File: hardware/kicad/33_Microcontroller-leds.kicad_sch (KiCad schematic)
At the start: 11 parts, among them U69 74AHCT1G125GW,125-JSM, U70 WS2815F, U71 VH3_96-4P_ZZ

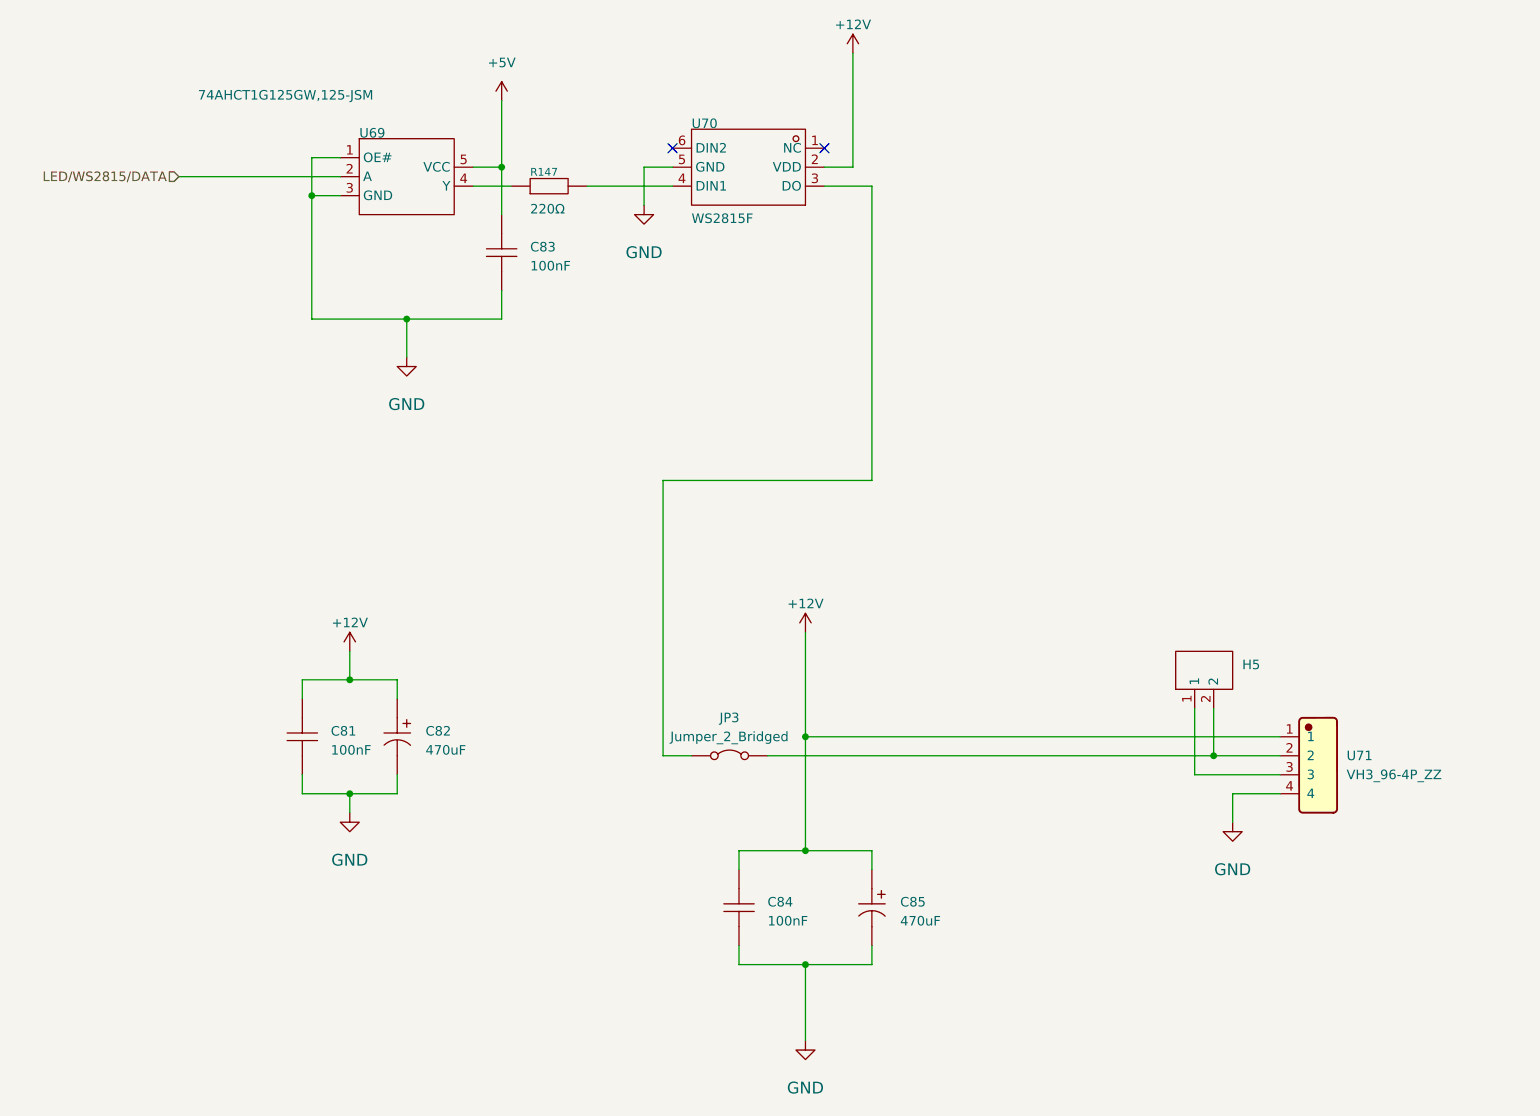
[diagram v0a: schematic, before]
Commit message: new led connector
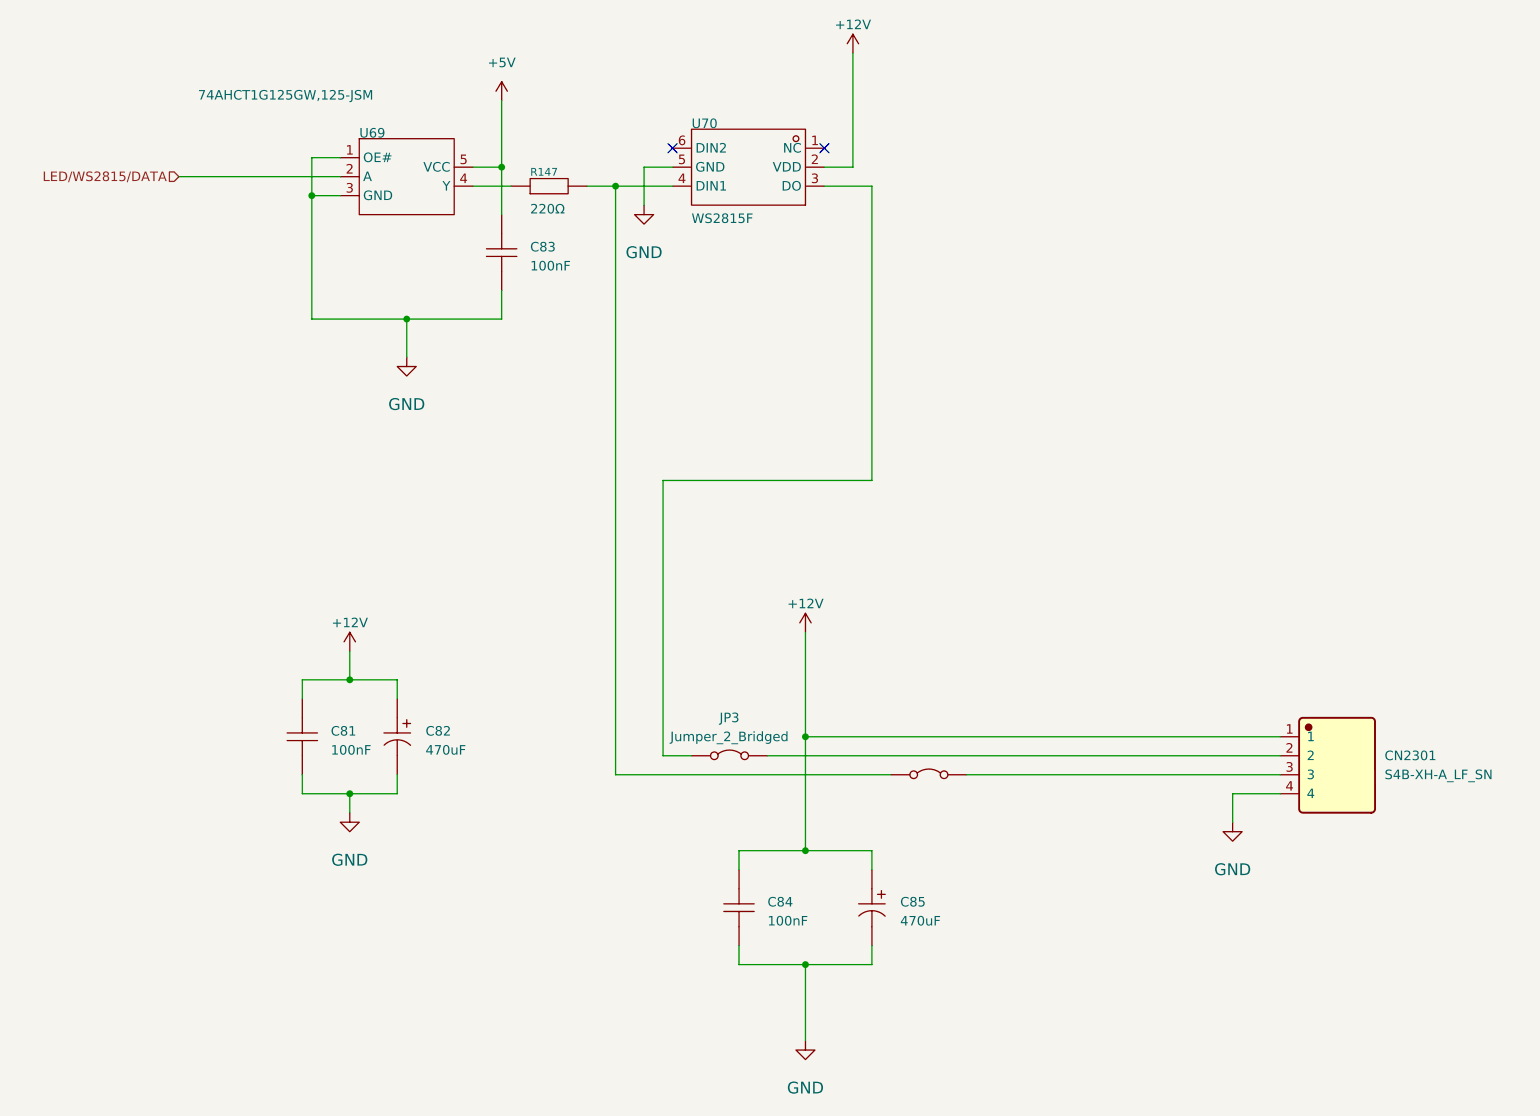
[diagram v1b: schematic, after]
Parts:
- removed H5: PZ254V-11-02P, Connector_PinHeader_2.54mm:PinHeader_1x02_P2.54mm_Vertical, symbol 5v rail sm-easyedapro:PZ254V-11-02P
- removed U71: VH3_96-4P_ZZ, JLCImport:VH3_96-4P_ZZ, symbol JLCImport:VH3_96-4P_ZZ
- added CN2301: S4B-XH-A_LF_SN, JLCImport:S4B-XH-A_LF_SN, symbol JLCImport:S4B-XH-A_LF_SN
- added JP2301: Jumper_2_Bridged, Jumper:SolderJumper-2_P1.3mm_Bridged_RoundedPad1.0x1.5mm, symbol Jumper:Jumper_2_Bridged
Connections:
- net +12V: now also CN2301.1
- net GND: now also CN2301.4
- net at JP3.2 (B): now also CN2301.2
- net at R147.2, U70.4 (DIN1): now also JP2301.1 (A)
- new net: CN2301.3, JP2301.2 (B)

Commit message: starting erc check
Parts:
- C81, C83, C84: footprint Capacitor_SMD:C_0603_1608Metric -> 5v rail sm-easyedapro:C0603
- R147: footprint Resistor_SMD:R_0603_1608Metric -> 5v rail sm-easyedapro:R0603
- U69: footprint Package_TO_SOT_SMD:SOT-353_SC-70-5 -> 5v rail sm-easyedapro:SOT-353_L2.1-W1.3-P0.65-LS2.3-BL
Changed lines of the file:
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@@
 			)
 		)
-		(property "Description" ""
+		(property "Description" "Power symbol creates a global label with name \"GND\" , ground"
 			(at 74.93 78.74 0)
 			(effects
@@
 			)
 		)
-		(property "Description" ""
+		(property "Description" "Power symbol creates a global label with name \"GND\" , ground"
 			(at 67.31 139.7 0)
 			(effects
@@
 			)
 		)
-		(property "Footprint" "Capacitor_SMD:C_0603_1608Metric"
+		(property "Footprint" "5v rail sm-easyedapro:C0603"
 			(at 60.96 129.54 0)
 			(effects
@@
 			)
 		)
-		(property "Footprint" "Package_TO_SOT_SMD:SOT-353_SC-70-5"
+		(property "Footprint" "5v rail sm-easyedapro:SOT-353_L2.1-W1.3-P0.65-LS2.3-BL"
 			(at 74.93 54.61 0)
 			(effects
@@
 			)
 		)
-		(property "Footprint" "Capacitor_SMD:C_0603_1608Metric"
+		(property "Footprint" "5v rail sm-easyedapro:C0603"
 			(at 87.63 64.77 0)
 			(effects
@@
 			)
 		)
-		(property "Footprint" "Resistor_SMD:R_0603_1608Metric"
+		(property "Footprint" "5v rail sm-easyedapro:R0603"
 			(at 93.98 55.88 0)
 			(effects
@@
 			)
 		)
-		(property "Description" ""
+		(property "Description" "Power symbol creates a global label with name \"GND\" , ground"
 			(at 185.42 140.97 0)
 			(effects
@@
 			)
 		)
-		(property "Description" ""
+		(property "Description" "Power symbol creates a global label with name \"GND\" , ground"
 			(at 128.27 170.18 0)
 			(effects
@@
 			)
 		)
-		(property "Footprint" "Capacitor_SMD:C_0603_1608Metric"
+		(property "Footprint" "5v rail sm-easyedapro:C0603"
 			(at 119.38 152.4 0)
 			(effects
@@
 			)
 		)
-		(property "Description" ""
+		(property "Description" "Power symbol creates a global label with name \"GND\" , ground"
 			(at 106.68 58.42 0)
 			(effects

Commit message: leds mostly done
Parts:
- removed C81: 100nF, 5v rail sm-easyedapro:C0603, symbol 5v rail sm-easyedapro:CC0603KRX7R9BB104
- removed C82: 470uF, 5v rail sm-easyedapro:CAP-SMD_BD6.3-L6.6-W6.6-LS7.6-RD, symbol 5v rail sm-easyedapro:RVT1C471M0607
- removed JP2301, JP3: Jumper_2_Bridged, Jumper:SolderJumper-2_P1.3mm_Bridged_RoundedPad1.0x1.5mm, symbol Jumper:Jumper_2_Bridged
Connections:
- net GND: now also C85.2
- net at U70.3 (DO): now also CN2301.3
- no-connect marks 2 -> 3

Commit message: updating symbols to use kicad footprints where possible
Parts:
- C83, C84: footprint 5v rail sm-easyedapro:C0603 -> Capacitor_SMD:C_0603_1608Metric
- R147: footprint 5v rail sm-easyedapro:R0603 -> Resistor_SMD:R_0603_1608Metric
- U69: footprint 5v rail sm-easyedapro:SOT-353_L2.1-W1.3-P0.65-LS2.3-BL -> Package_TO_SOT_SMD:SOT-353_SC-70-5
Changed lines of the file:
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@@
 			)
 		)
-		(property "Footprint" "5v rail sm-easyedapro:SOT-353_L2.1-W1.3-P0.65-LS2.3-BL"
+		(property "Footprint" "Package_TO_SOT_SMD:SOT-353_SC-70-5"
 			(at 74.93 54.61 0)
 			(effects
@@
 			)
 		)
-		(property "Footprint" "5v rail sm-easyedapro:C0603"
+		(property "Footprint" "Capacitor_SMD:C_0603_1608Metric"
 			(at 87.63 64.77 0)
 			(effects
@@
 			)
 		)
-		(property "Footprint" "5v rail sm-easyedapro:R0603"
+		(property "Footprint" "Resistor_SMD:R_0603_1608Metric"
 			(at 93.98 55.88 0)
 			(effects
@@
 			)
 		)
-		(property "Footprint" "5v rail sm-easyedapro:C0603"
+		(property "Footprint" "Capacitor_SMD:C_0603_1608Metric"
 			(at 119.38 152.4 0)
 			(effects

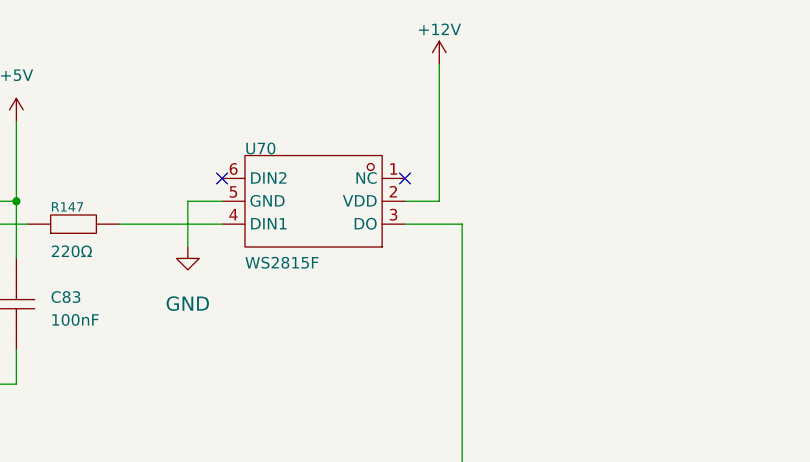
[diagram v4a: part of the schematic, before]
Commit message: starting erc check
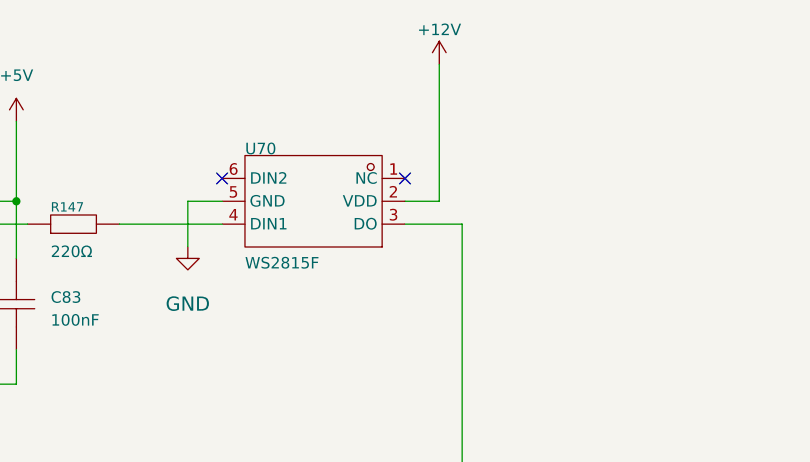
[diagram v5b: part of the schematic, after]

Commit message: more fixes
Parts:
- U70: footprint 5v rail sm-easyedapro:LED-SMD_6P-L5.0-W5.0-TL -> LED_SMD:LED_WS2812_PLCC6_5.0x5.0mm_P1.6mm
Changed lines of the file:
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@@
 			)
 		)
-		(property "Footprint" "5v rail sm-easyedapro:LED-SMD_6P-L5.0-W5.0-TL"
+		(property "Footprint" "LED_SMD:LED_WS2812_PLCC6_5.0x5.0mm_P1.6mm"
 			(at 120.65 53.34 0)
 			(effects

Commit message: update
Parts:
- removed C85: 470uF, 5v rail sm-easyedapro:CAP-SMD_BD6.3-L6.6-W6.6-LS7.6-RD, symbol 5v rail sm-easyedapro:RVT1C471M0607
- added C2301: 189RV0019, JLCImport:189RV0019, symbol JLCImport:189RV0019
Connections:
- net +12V: now also C2301.1
- net GND: now also C2301.2
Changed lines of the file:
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@@
-	)
-	(symbol
-		(lib_id "5v rail sm-easyedapro:RVT1C471M0607")
-		(at 137.16 152.4 270)
-		(unit 1)
-		(exclude_from_sim no)
-		(in_bom yes)
-		(on_board yes)
-		(dnp no)
-		(property "Reference" "C85"
-			(at 140.9446 152.4 90)
-			(effects
-				(font
-					(size 1.27 1.27)
-				)
-				(justify left bottom)
-			)
-		)
-		(property "Value" "470uF"
-			(at 140.9446 154.94 90)
-			(effects
-				(font
-					(size 1.27 1.27)
-				)
-				(justify left bottom)
-			)
-		)
-		(property "Footprint" "5v rail sm-easyedapro:CAP-SMD_BD6.3-L6.6-W6.6-LS7.6-RD"
-			(at 137.16 152.4 0)
-			(effects
-				(font
-					(size 1.27 1.27)
-				)
-				(hide yes)
-			)
-		)
-		(property "Datasheet" ""
-			(at 137.16 152.4 0)
-			(effects
-				(font
-					(size 1.27 1.27)
-				)
-				(hide yes)
-			)
-		)
-		(property "Description" "Capacitance:470uF Tolerance:±20% Tolerance:±20% Voltage Rating:16V Ripple Current:185mA@120Hz Diameter:6.3mm Height - Seated (Max):7.7mm Lifetime:2000hrs@105°C Operating Temperature:-40°C~+105°C Operating Temperature:-40°C~+105°C"
-			(at 137.16 152.4 0)
-			(effects
-				(font
-					(size 1.27 1.27)
-				)
-				(hide yes)
-			)
-		)
-		(property "Manufacturer Part" "RVT1C471M0607"
-			(at 137.16 152.4 0)
-			(effects
-				(font
-					(size 1.27 1.27)
-				)
-				(hide yes)
-			)
-		)
-		(property "Manufacturer" "ROQANG(容强)"
-			(at 137.16 152.4 0)
-			(effects
-				(font
-					(size 1.27 1.27)
-				)
-				(hide yes)
-			)
-		)
-		(property "Supplier Part" "C2977552"
-			(at 137.16 152.4 0)
-			(effects
-				(font
-					(size 1.27 1.27)
-				)
-				(hide yes)
-			)
-		)
-		(property "Supplier" "LCSC"
-			(at 137.16 152.4 0)
-			(effects
-				(font
-					(size 1.27 1.27)
-				)
-				(hide yes)
-			)
-		)
-		(property "LCSC Part Name" "470uF ±20% 16V"
-			(at 137.16 152.4 0)
-			(effects
-				(font
-					(size 1.27 1.27)
-				)
-				(hide yes)
-			)
-		)
-		(pin "1"
-		)
-		(pin "2"
-		)
-		(instances
-			(project "svea_powerboard_rev3"
-				(path "/3f85abf4-0b95-4c4a-b7e9-06f59ca1ea3d/5c2e021f-c2d4-49e2-8c36-9a64f1f12001/c2eb7228-bcb6-49cd-ba01-e5b0712a5c09"
-					(reference "C85")
-					(unit 1)
-				)
-			)
-		)
 	)
 	(symbol
@@
 					(unit 1)
 				)
+			)
+		)
+	)
+	(symbol
+		(lib_id "JLCImport:189RV0019")
+		(at 137.16 152.4 270)
+		(unit 1)
+		(exclude_from_sim no)
+		(in_bom yes)
+		(on_board yes)
+		(dnp no)
+		(fields_autoplaced yes)
+		(property "Reference" "C2301"
+			(at 140.97 151.1299 90)
+			(effects
+				(font
+					(size 1.27 1.27)
+				)
+				(justify left)
+			)
+		)
+		(property "Value" "189RV0019"
+			(at 140.97 153.6699 90)
+			(effects
+				(font
+					(size 1.27 1.27)
+				)
+				(justify left)
+			)
+		)
+		(property "Footprint" "JLCImport:189RV0019"
+			(at 137.16 152.4 0)
+			(effects
+				(font
+					(size 1.27 1.27)
+				)
+				(hide yes)
+			)
+		)
+		(property "Datasheet" "https://wmsc.lcsc.com/wmsc/upload/file/pdf/v2/lcsc/2309071525_KNSCHA-189RV0019_C7471881.pdf"
+			(at 137.16 152.4 0)
+			(effects
+				(font
+					(size 1.27 1.27)
+				)
+				(hide yes)
+			)
+		)
+		(property "Description" "-55℃~+105℃ 160mΩ@100KHz 2000hrs@105℃ 220uF 35V 6.3mm 600mA@100KHz 7.7mm ±20% SMD,D6.3xL7.7mm Aluminum Electrolytic Capacitors - SMD ROHS"
+			(at 137.16 152.4 0)
+			(effects
+				(font
+					(size 1.27 1.27)
+				)
+				(hide yes)
+			)
+		)
+		(property "LCSC" "C7471881"
+			(at 137.16 152.4 0)
+			(effects
+				(font
+					(size 1.27 1.27)
+				)
+				(hide yes)
+			)
+		)
+		(property "Manufacturer" "KNSCHA"
+			(at 137.16 152.4 0)
+			(effects
+				(font
+					(size 1.27 1.27)
+				)
+				(hide yes)
+			)
+		)
+		(property "Manufacturer Part" "189RV0019"
+			(at 137.16 152.4 0)
+			(effects
+				(font
+					(size 1.27 1.27)
+				)
+				(hide yes)
+			)
+		)
+		(pin "1"
+		)
+		(pin "2"
+		)
+		(instances
+			(project ""
+				(path "/3f85abf4-0b95-4c4a-b7e9-06f59ca1ea3d/5c2e021f-c2d4-49e2-8c36-9a64f1f12001/c2eb7228-bcb6-49cd-ba01-e5b0712a5c09"
+					(reference "C2301")
+					(unit 1)
+				)

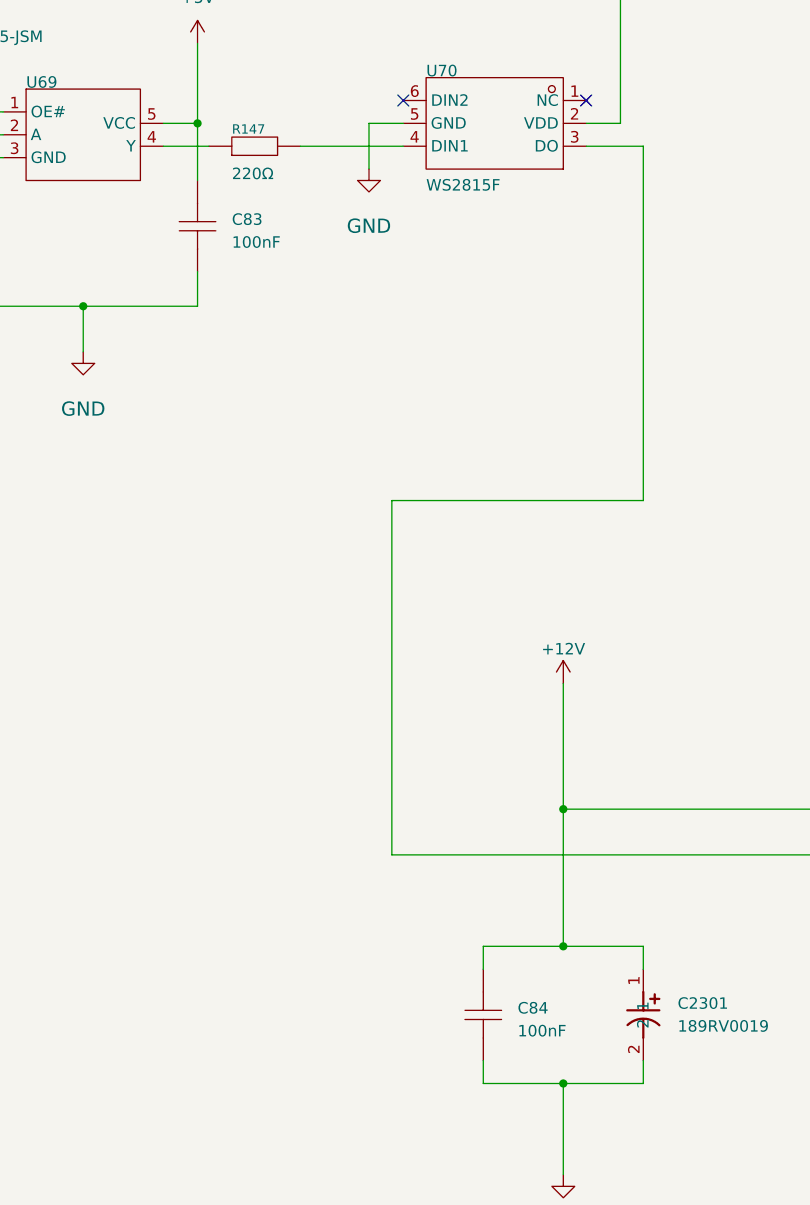
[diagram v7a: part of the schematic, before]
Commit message: fixing inconsistencies in value convention
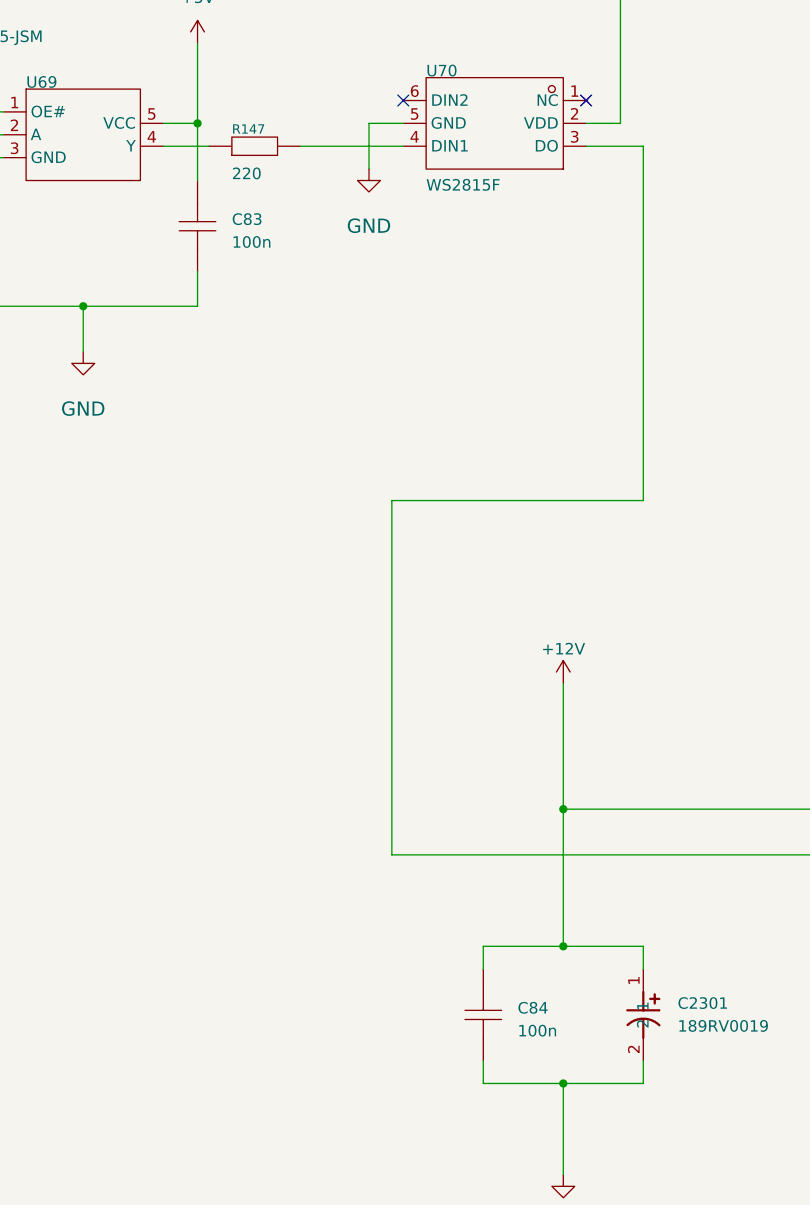
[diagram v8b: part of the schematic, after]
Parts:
- C83, C84: value 100nF -> 100n
- R147: value 220Ω -> 220
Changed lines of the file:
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@@
 			)
 		)
-		(property "Value" "100nF"
+		(property "Value" "100n"
 			(at 91.44 67.31 90)
 			(effects
@@
 			)
 		)
-		(property "Value" "220Ω"
+		(property "Value" "220"
 			(at 91.44 59.69 0)
 			(effects
@@
 			)
 		)
-		(property "Value" "100nF"
+		(property "Value" "100n"
 			(at 123.19 154.94 90)
 			(effects
